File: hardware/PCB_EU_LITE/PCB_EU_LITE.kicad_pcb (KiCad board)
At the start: 4 copper layers, 100 x 100 mm, 165 parts, among them J101 24 V IN, J201 UART 3V3, J301 MEM2061 SPI, J401 SHT4x XH2.54-4P-90, J403 FLOAT / GND, J411 FAN1 2510-4P, J421 FAN2 2510-4P, J501 LED + / GND, J701 PTC + / RETURN, J702 PUMP + / RETURN, Q102 IRL2505, Q411 FAN1 AO3422, Q421 FAN2 AO3422, Q501 BSC146N10LS5, Q701 BC847B-DIO, Q702 BC857B, Q703 BSC146N10LS5, Q704 AO3422, Q901 BC847B (R), Q902 BC847B (G), Q903 BC847B (B), SW201 RESET, SW202 BOOT, U101 ST1S14PHR, U102 INA238, U201 ST1S10PHR, U202 ESP32-WROOM-32E-N4, U301 MCP7940N, U401 USBLC6-2SC6, U501 LM3429MH/NOPB, Y301 32.768k CL7p

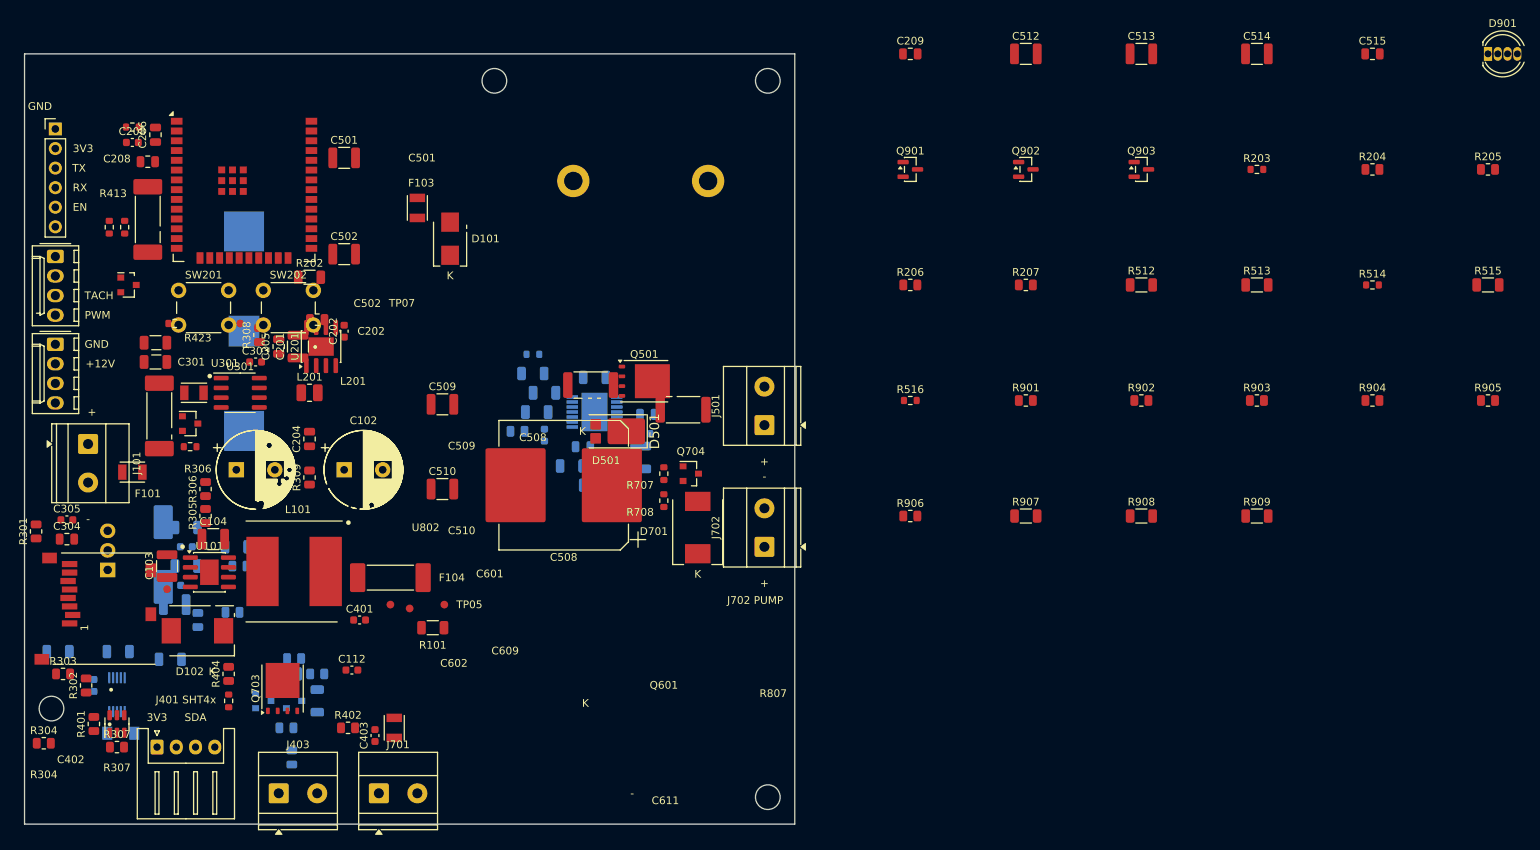
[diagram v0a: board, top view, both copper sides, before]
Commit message: Place EU-LITE components on top with the battery underneath
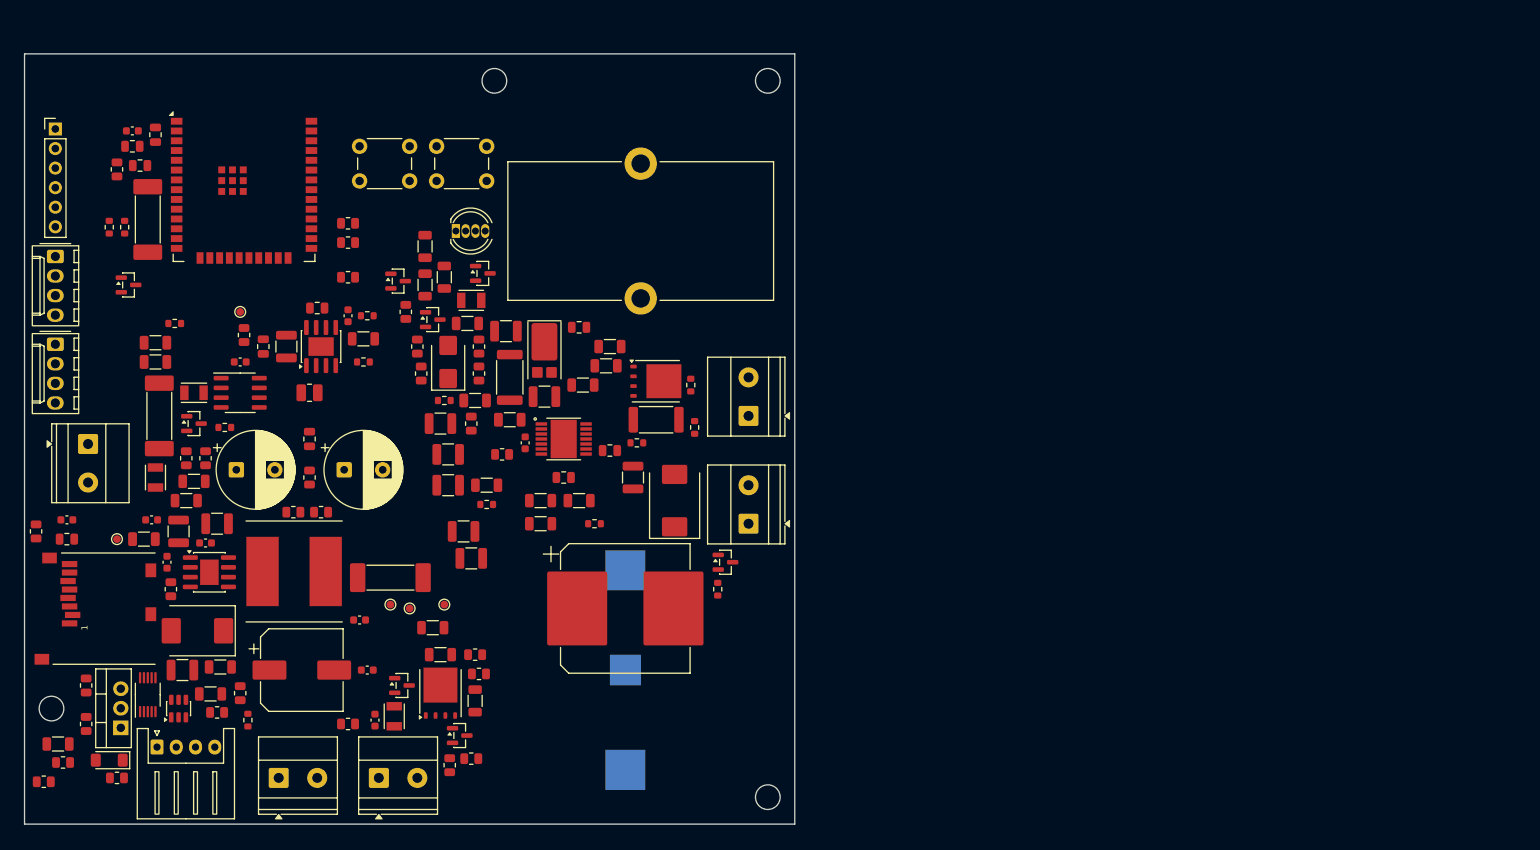
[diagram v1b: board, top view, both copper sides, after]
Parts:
- C105, C106, C107, C110, C111, C115, C503, C504, C505, C506, C507, C511, D103, L501, Q102, Q701, Q702, R102, R103, R104, R105, R106, R107, R108, R111, R112, R503, R504, R505, R506, R507, R508, R509, R510, R511, R701, R702, R703, R704, R705, R706, U102, U501: moved to F.Cu
- moved R204 163.0 mm to (12.0, 15.0), turned to 90 degrees
- moved R205 148.7 mm to (42.0, 29.0)
- moved R905 138.5 mm to (51.5, 41.5), turned to 90 degrees
- moved D901 136.0 mm to (56.0, 23.0)
- moved R515 132.6 mm to (60.0, 56.0)
- moved R904 124.2 mm to (51.0, 38.0), turned to 90 degrees
- moved C514 121.2 mm to (58.0, 65.5)
- moved R203 118.7 mm to (44.0, 40.0)
- moved R909 112.1 mm to (52.0, 30.0), turned to 90 degrees
- moved C515 108.9 mm to (72.0, 35.5)
- moved C513 107.6 mm to (57.0, 62.0)
- moved R903 101.2 mm to (59.0, 38.0), turned to 90 degrees
- moved C209 101.0 mm to (15.0, 14.5)
- moved R908 95.7 mm to (54.5, 29.0), turned to 90 degrees
- moved C512 93.6 mm to (55.0, 56.0)
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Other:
- board text added: "EU-LITE / UNROUTED / 100 x 100 mm / 4 Cu / NOT FOR FABRICATION"
- board text removed: "+"
- board text removed: "+12V"
- board text removed: "-"
- board text removed: "3V3"
- board text removed: "BOOT"
- board text removed: "BT301"
- board text removed: "BT301 CR2032"
- board text removed: "C102"
- board text removed: "C202"
- board text removed: "C208"
- board text removed: "C301"
- board text removed: "C402"
- board text removed: "C501"
- board text removed: "C502"
- board text removed: "C503"
- board text removed: "C504"
- board text removed: "C508"
- board text removed: "C509"
- board text removed: "C510"
- board text removed: "C511"
- board text removed: "C601"
- board text removed: "C602"
- board text removed: "C609"
- board text removed: "C611"
- board text removed: "C803"
- board text removed: "D101"
- board text removed: "D102"
- board text removed: "D103"
- board text removed: "D501"
- board text removed: "D701"
- board text removed: "EN"
- board text removed: "EU-0.1 / ROUTED, NOT RELEASED / 100 x 100 mm / 4 Cu"
- board text removed: "F101"
- board text removed: "F103"
- board text removed: "F104"
- board text removed: "F106"
- board text removed: "GND"
- board text removed: "HS1 RESERVE ONLY"
- board text removed: "HS1 on two soldered GND pins / clamping, physical fit and thermal NOT qualified"
- board text removed: "J101 24V IN"
- board text removed: "J201 UART"
- board text removed: "J401 SHT4x"
- board text removed: "J411 FAN1"
- board text removed: "J421 FAN2"
- board text removed: "J501 LED1"
- board text removed: "J601 LED2"
- board text removed: "J602 LED2 BAR2"
- board text removed: "J701 PTC"
- board text removed: "J702 PUMP"
- board text removed: "K"
- board text removed: "L101"
- board text removed: "L201"
- board text removed: "L501"
- board text removed: "L502"
- board text removed: "L601"
- board text removed: "PWM"
- board text removed: "Q102"
- board text removed: "Q601"
- board text removed: "Q702"
- board text removed: "Q704"
- board text removed: "R101"
- board text removed: "R102"
- board text removed: "R103"
- board text removed: "R104"
- board text removed: "R105"
- board text removed: "R106"
- board text removed: "R107"
- board text removed: "R108"
- board text removed: "R113"
- board text removed: "R304"
- board text removed: "R306"
- board text removed: "R307"
- board text removed: "R413"
- board text removed: "R423"
- board text removed: "R503"
- board text removed: "R504"
- board text removed: "R508"
- board text removed: "R509"
- board text removed: "R510"
- board text removed: "R511"
- board text removed: "R604"
- board text removed: "R606"
- board text removed: "R609"
- board text removed: "R611"
- board text removed: "R701"
- board text removed: "R702"
- board text removed: "R703"
- board text removed: "R704"
- board text removed: "R705"
- board text removed: "R706"
- board text removed: "R707"
- board text removed: "R708"
- board text removed: "R804"
- board text removed: "R807"
- board text removed: "R808"
- board text removed: "R810"
- board text removed: "R811"
- board text removed: "R813"
- board text removed: "R817"
- board text removed: "RX"
- board text removed: "SCL"
- board text removed: "SDA"
- board text removed: "SIG"
- board text removed: "TACH"
- board text removed: "TP05"
- board text removed: "TP07"
- board text removed: "TX"
- board text removed: "U301"
- board text removed: "U802"

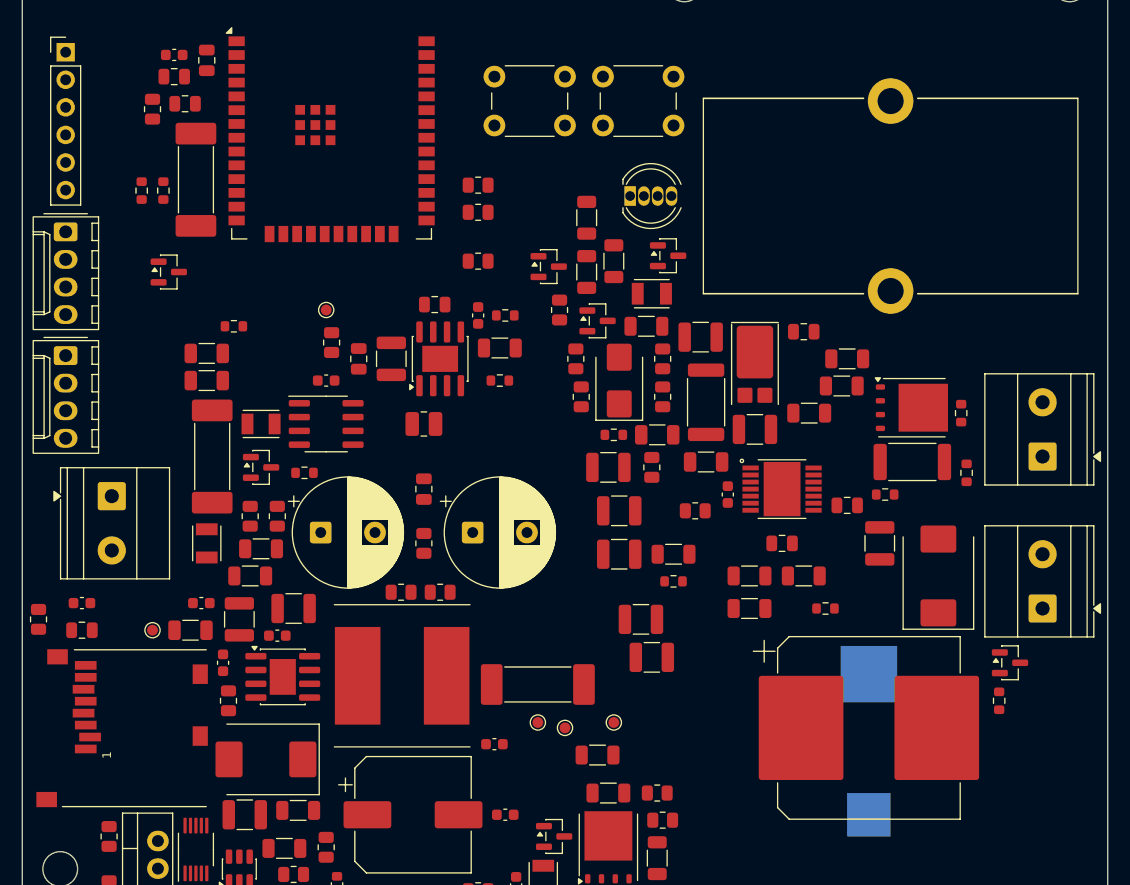
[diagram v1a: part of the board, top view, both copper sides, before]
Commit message: Move EU-LITE connectors to edges and add right-angle fan headers
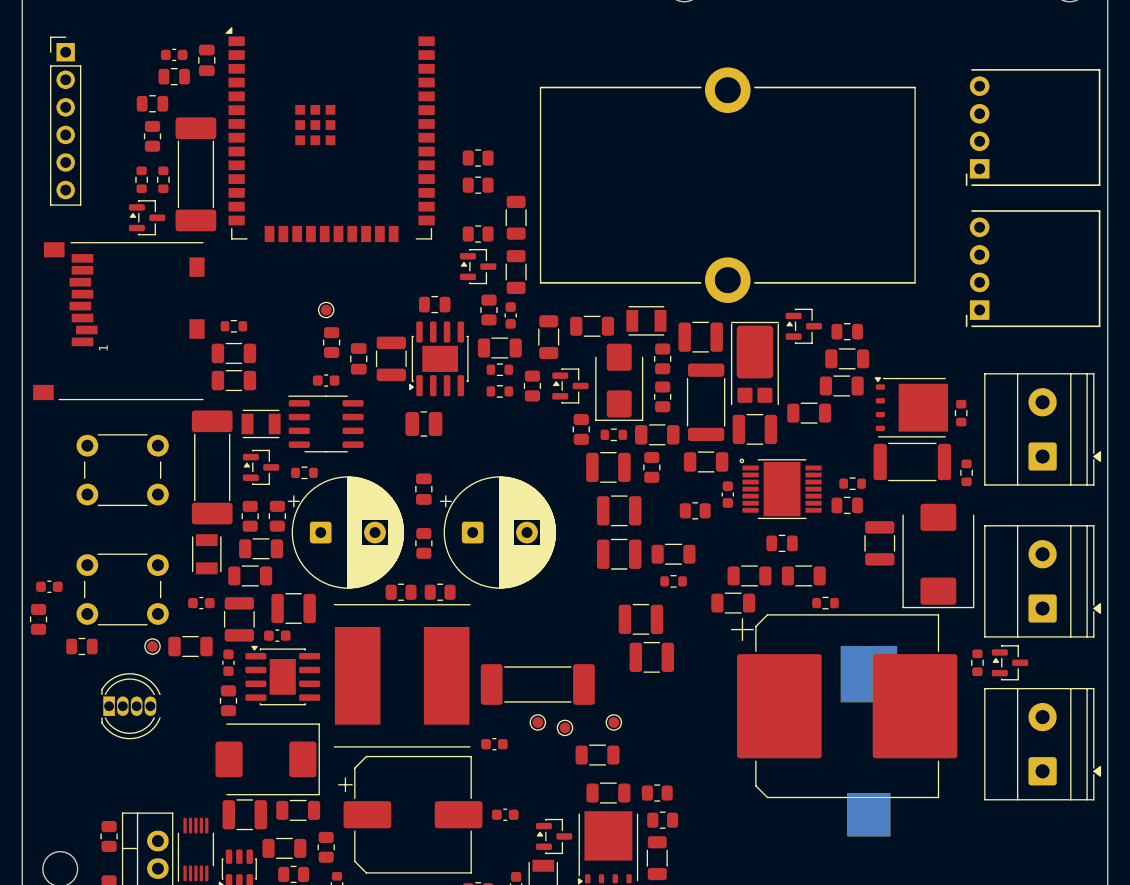
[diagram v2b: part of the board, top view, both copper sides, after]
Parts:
- J411: value FAN1 2510-4P -> FAN1 2510-4P 90deg; footprint Connector_Molex:Molex_KK-254_AE-6410-04A_1x04_P2.54mm_Vertical -> LITE_Parts:KF2510_1x04_P2.54mm_RightAngle
- J421: value FAN2 2510-4P -> FAN2 2510-4P 90deg; footprint Connector_Molex:Molex_KK-254_AE-6410-04A_1x04_P2.54mm_Vertical -> LITE_Parts:KF2510_1x04_P2.54mm_RightAngle
- moved J101 89.4 mm to (94.0, 76.0), turned to 90 degrees
- moved J411 84.4 mm to (88.2, 20.5), turned to 90 degrees
- moved J421 84.3 mm to (88.2, 33.5), turned to 90 degrees
- moved D901 67.2 mm to (8.00, 70.0)
- moved SW202 65.4 mm to (6.00, 57.0)
- moved SW201 50.6 mm to (6.00, 46.0)
- moved J301 37.5 mm to (16.5, 27.5)
- moved L501 15.0 mm to (65.0, 22.0)
- moved Q903 14.1 mm to (72.0, 35.0)
- moved R908 9.06 mm to (45.5, 30.0)
- moved R909 6.95 mm to (48.5, 36.0)
- moved Q901 6.50 mm to (42.0, 29.5)
- moved Q902 6.50 mm to (50.5, 40.5)
- moved R901 6.50 mm to (43.0, 33.5)
- moved R907 6.50 mm to (45.5, 25.0)
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
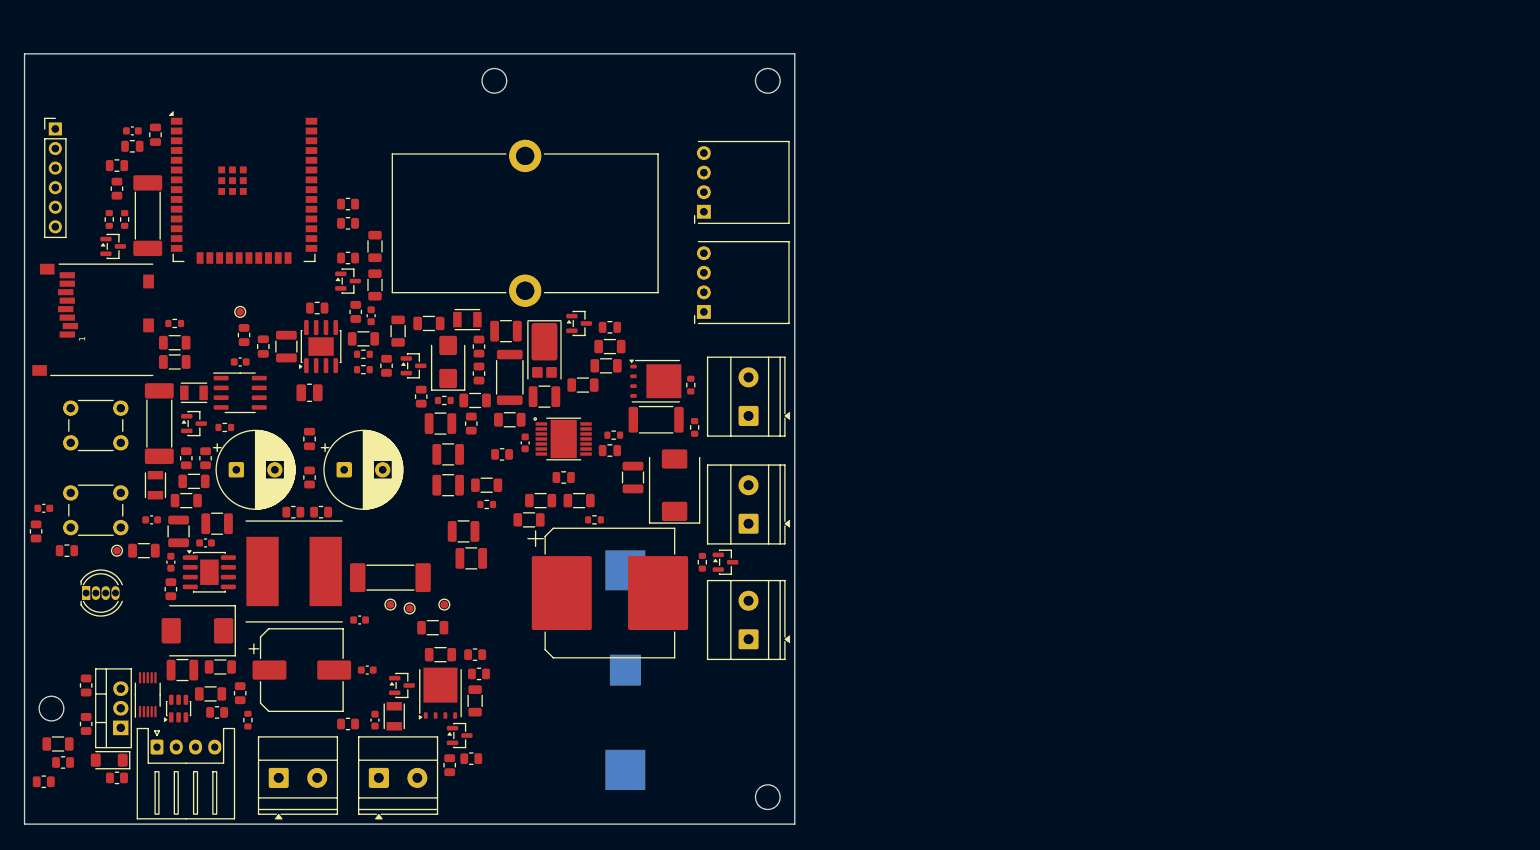
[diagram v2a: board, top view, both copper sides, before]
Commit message: Refine EU-LITE placement and select RGB LED
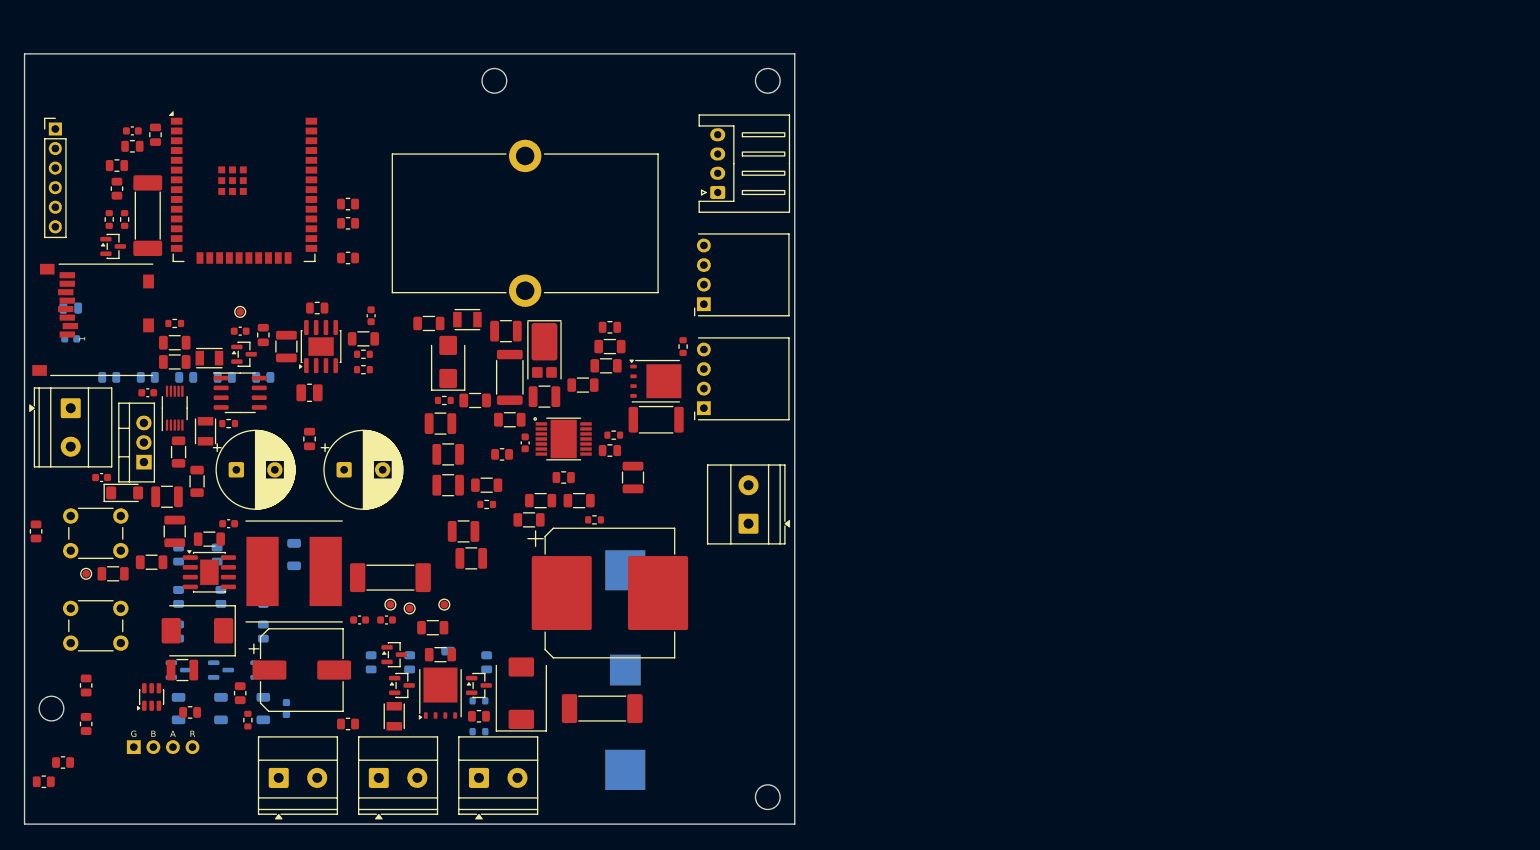
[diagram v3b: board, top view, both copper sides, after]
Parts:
- C304, C305, C403, Q901, Q902, Q903, R104, R105, R106, R107, R305, R306, R307, R308, R309, R701, R702, R703, R704, R707, R708, R901, R902, R903, R904, R905, R906, R907, R908, R909: moved to B.Cu
- D901: value RGB 5mm CA -> OSTAPA57E2A; footprint LED_THT:LED_D5.0mm-4_RGB -> LITE_Parts:LED_OSTAPA57E2A_Formed_P2.54mm
- moved J401 102.4 mm to (90.0, 18.0), turned to 90 degrees
- moved J101 93.0 mm to (6.00, 46.0), turned to -90 degrees
- moved F105 68.4 mm to (75.0, 85.0), turned to 0 degrees
- moved R907 65.2 mm to (20.0, 85.0)
- moved Q903 60.9 mm to (31.0, 80.0)
- moved R908 58.5 mm to (25.5, 85.0)
- moved Q901 55.1 mm to (20.0, 80.0)
- moved R307 52.8 mm to (21.0, 42.0)
- moved R909 52.0 mm to (31.0, 85.0)
- moved J702 48.1 mm to (59.0, 94.0), turned to 0 degrees
- moved R901 47.4 mm to (20.0, 75.0)
- moved R902 47.4 mm to (25.5, 75.0)
- moved Q902 46.7 mm to (25.5, 80.0)
- moved R903 46.4 mm to (31.0, 75.0)
- moved R707 45.2 mm to (59.0, 84.0), turned to 0 degrees
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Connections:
- D901 pad 1: LED_R_K -> LED_G_K
- D901 pad 2: +12V -> LED_B_K
- D901 pad 3: LED_G_K -> +12V
- D901 pad 4: LED_B_K -> LED_R_K
